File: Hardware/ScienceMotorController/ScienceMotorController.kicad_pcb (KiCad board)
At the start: 2 copper layers, 124.5 x 108.5 mm, 128 parts, among them SW1 Molex_SL_02, SW2 Molex_SL_02, SW3 Molex_SL_02, SW4 Molex_SL_02, SW5 Molex_SL_02, SW6 Molex_SL_02, U1 LT1910, U10 PMN280ENEAX, U11 TB67H400AFNG,EL, U12 TB67H400AFNG,EL, U13 LT1910, U14 PMN280ENEAX, U15 LTC6900, U16 TB67H400AFNG,EL, U17 TB67H400AFNG,EL, U2 OKI, U3 OKI, U4 OKI, U5 TB67H400AFNG,EL, U6 TB67H400AFNG,EL, U7 PMN280ENEAX, U8 LT1910, U9 TM4C129E_Launchpad

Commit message: deleted extra LEDs and Resistors. Generated and loaded new netlist.
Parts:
- removed D13, D21, D3, D6: LED, LED_SMD:LED_0603_1608Metric_Pad1.05x0.95mm_HandSolder
- removed R13, R23, R36: 3.3k, Resistor_SMD:R_0603_1608Metric_Pad1.05x0.95mm_HandSolder
- removed R4: 330, Resistor_SMD:R_0603_1608Metric_Pad1.05x0.95mm_HandSolder
- moved D16 128.3 mm to (125.2, 95.4), turned to 270 degrees
- moved D15 0.25 mm to (144.7, 96.0)
- moved R21 0.25 mm to (144.7, 92.5)
- renumbered Encode1 to AbsEncode1, Encode2 to AbsEncode2, Encode3 to AbsEncode3, Encode4 to AbsEncode4, Encode5 to AbsEncode5, SW1 to LimSwitch1, SW2 to LimSwitch2, SW3 to LimSwitch3, SW4 to LimSwitch4, SW5 to LimSwitch5, SW6 to LimSwitch6
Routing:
- net Net-(Conn2-Pad2): track 24.8 -> 23.5 mm

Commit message: more connections made, beginning to connect moco ICs
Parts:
- added REF**: 4_40_Hole, MRDT_Drill_Holes:4_40_Hole_Corner, F.Cu at (147.1, 84.3)
- added REF**: 4_40_Hole, MRDT_Drill_Holes:4_40_Hole_Corner, F.Cu at (38.8, 84.3)
- added REF**: 4_40_Hole, MRDT_Drill_Holes:4_40_Hole_Corner, F.Cu at (147.2, 176.6)
- added REF**: 4_40_Hole, MRDT_Drill_Holes:4_40_Hole_Corner, F.Cu at (38.8, 176.6)
- moved R8 293.3 mm to (21.3, 96.1)
- moved R7 236.5 mm to (21.1, 99.4)
- moved C9 216.9 mm to (83.4, 146.2), turned to 270 degrees
- moved R31 186.4 mm to (99.9, 146.2), turned to 270 degrees
- moved R22 181.5 mm to (128.8, 92.0), turned to 270 degrees
- moved R5 166.0 mm to (63.4, 152.7), turned to 180 degrees
- moved C11 165.1 mm to (98.2, 146.2), turned to 270 degrees
- moved R20 160.3 mm to (85.2, 146.2), turned to 270 degrees
- moved D4 149.5 mm to (66.9, 152.7), turned to 180 degrees
- moved R14 108.5 mm to (186.1, 150.0), turned to 90 degrees
- moved D7 106.7 mm to (184.3, 150.0), turned to 270 degrees
- moved R24 97.5 mm to (189.3, 159.4), turned to 180 degrees
- moved D14 97.3 mm to (189.4, 157.6), turned to 0 degrees
- moved R17 71.2 mm to (63.4, 154.3)
- moved D10 67.9 mm to (66.9, 154.3), turned to 180 degrees
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- renumbered LimSwitch2 to SW2, LimSwitch3 to SW3, LimSwitch5 to SW5, LimSwitch6 to SW6, LimSwitch1 to SW`1, LimSwitch4 to Sw45
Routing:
- net +5VA: track 25.1 -> 90.4 mm, vias 1 -> 2
- net +5V: track 204.5 -> 254.4 mm, vias 11 -> 15
- net +12V: track 154.0 -> 158.8 mm, vias 3 -> 5
- net Net-(R37-Pad2): track 4.01 -> 0.20 mm
- net Limit_Switch_1: track 115.8 -> 112.1 mm
- net Net-(R24-Pad2): track 3.61 -> 0.00 mm
- net Net-(R14-Pad2): track 3.56 -> 0.00 mm
- net +3V3: track 115.7 -> 119.1 mm
- net Oscillator: track 141.9 -> 139.2 mm, vias 10 -> 8
- net Net-(C9-Pad1): track 0.00 -> 2.56 mm
- net Net-(C11-Pad1): track 0.00 -> 2.56 mm
- net Limit_Switch_2: track 111.5 -> 109.0 mm
- net Net-(R20-Pad1): track 0.00 -> 2.41 mm
- net Net-(R31-Pad1): track 0.00 -> 2.35 mm
- net Net-(D16-Pad1): track 0.00 -> 2.03 mm
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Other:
- outline, holes or cut-outs redrawn
- board text added: "+12V"
- board text added: "+3V3"
- board text added: "+5V"
- board text added: "+5VA"
- board text added: "Power Indicators"
- board text removed: "+3V3 Indicator"
- board text removed: "+5V Indicator"
- board text removed: "+5VA Indicator"

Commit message: resistors on moco chips added.
Had changed netlist to try a different placement for the motor LEDs, but reverted to original position
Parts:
- removed REF** (x4): 4_40_Hole, MRDT_Drill_Holes:4_40_Hole_Corner
- moved D1 230.0 mm to (54.5, 97.8), turned to 180 degrees
- moved R45 221.8 mm to (72.2, 104.9)
- moved R1 221.0 mm to (54.5, 99.6)
- moved R46 212.5 mm to (72.2, 103.1)
- moved R41 211.3 mm to (72.2, 99.6)
- moved R9 210.2 mm to (54.5, 101.3)
- moved R40 199.9 mm to (90.5, 99.6)
- moved R47 196.5 mm to (72.2, 101.3)
- moved R44 194.3 mm to (90.5, 101.3)
- moved R11 189.2 mm to (109.0, 103.1)
- moved R30 187.4 mm to (127.4, 101.3)
- moved R2 181.3 mm to (109.0, 99.6)
- moved D26 177.9 mm to (72.2, 97.8), turned to 180 degrees
- moved R10 174.6 mm to (109.0, 104.9)
- moved R28 170.5 mm to (127.4, 104.9)
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- renumbered SW`1 to LimSwitch1, SW2 to LimSwitch2, SW3 to LimSwitch3, Sw45 to LimSwitch4, SW5 to LimSwitch5, SW6 to LimSwitch6
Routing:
- net +5V: track 254.4 -> 164.5 mm
- net Oscillator: track 139.2 -> 52.2 mm, vias 8 -> 7
- net GND: track 169.7 -> 182.5 mm
- net Net-(Conn4-Pad1): track 8.59 -> 20.1 mm
- net Net-(R7-Pad1): track 0.00 -> 3.23 mm
- net Net-(R10-Pad1): track 0.00 -> 3.21 mm
- net Net-(R28-Pad1): track 0.00 -> 3.09 mm
- net Net-(R25-Pad1): track 0.00 -> 3.03 mm
- net Net-(R26-Pad1): track 0.00 -> 3.01 mm
- net Net-(R45-Pad1): track 0.00 -> 2.98 mm
- net Net-(R42-Pad1): track 0.00 -> 2.96 mm
- net Net-(Conn6-Pad2): track 20.4 -> 23.1 mm
- net Net-(Conn1-Pad2): track 21.4 -> 24.2 mm
- net Net-(R47-Pad1): track 0.00 -> 2.66 mm
- net Net-(R30-Pad1): track 0.00 -> 2.63 mm
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
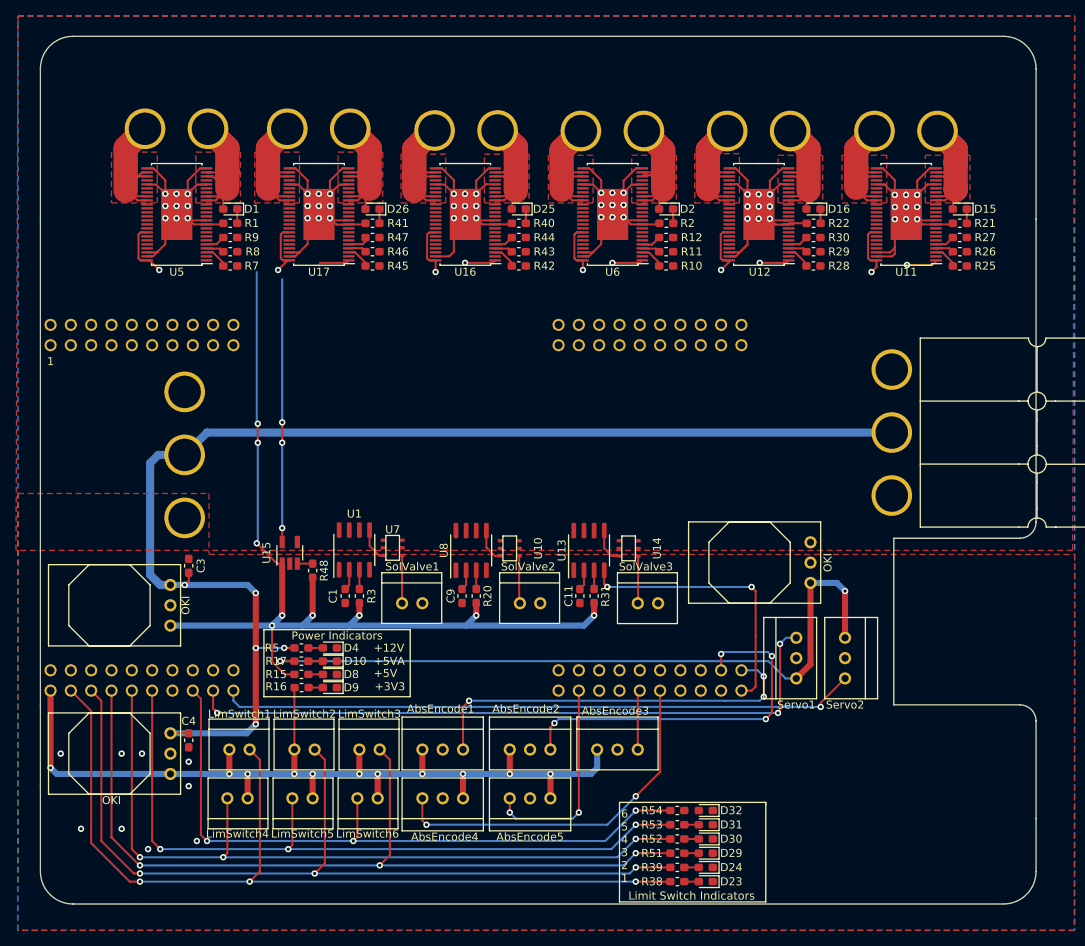
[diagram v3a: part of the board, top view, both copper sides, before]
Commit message: finished moco alignment
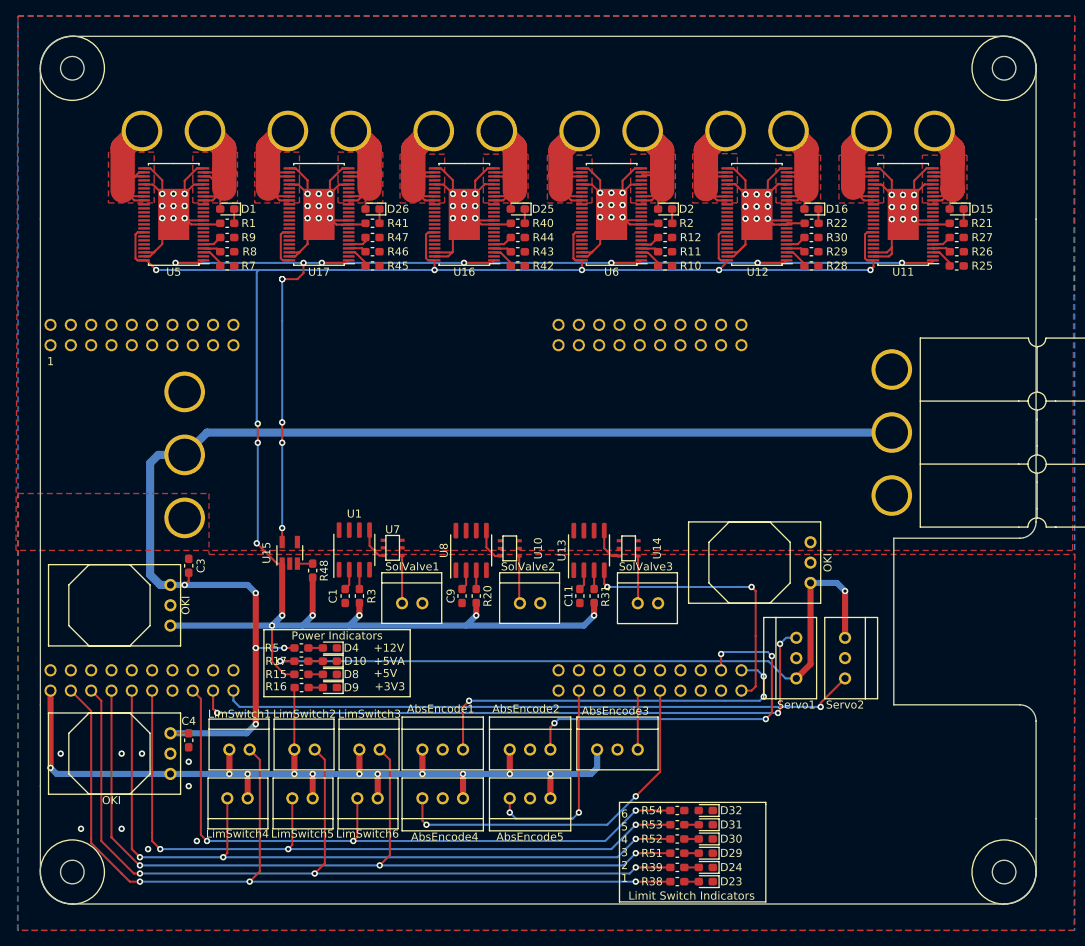
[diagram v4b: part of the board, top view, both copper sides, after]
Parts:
- added REF**: 4_40_Hole, MRDT_Drill_Holes:4_40_Hole_Corner, F.Cu at (147.2, 176.7)
- added REF**: 4_40_Hole, MRDT_Drill_Holes:4_40_Hole_Corner, F.Cu at (38.7, 176.7)
- added REF**: 4_40_Hole, MRDT_Drill_Holes:4_40_Hole_Corner, F.Cu at (38.7, 84.2)
- added REF**: 4_40_Hole, MRDT_Drill_Holes:4_40_Hole_Corner, F.Cu at (147.2, 84.2)
- moved Conn1 0.47 mm to (43.4, 88.0)
- moved Conn2 0.38 mm to (134.6, 88.0)
- moved D1 0.38 mm to (54.1, 97.8)
- moved D15 0.38 mm to (145.3, 97.8)
- moved R1 0.38 mm to (54.1, 99.6)
- moved R21 0.38 mm to (145.3, 99.6)
- moved R25 0.38 mm to (145.3, 104.9)
- moved R26 0.38 mm to (145.3, 103.1)
- moved R27 0.38 mm to (145.3, 101.3)
- moved R7 0.38 mm to (54.1, 104.9)
- moved R8 0.38 mm to (54.1, 103.1)
- moved R9 0.38 mm to (54.1, 101.3)
- moved U11 0.38 mm to (138.6, 98.5)
- moved U5 0.38 mm to (47.4, 98.5)
- moved Conn6 0.29 mm to (61.7, 88.0)
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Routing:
- net Oscillator: track 52.2 -> 151.0 mm, vias 7 -> 12
- net +5V: track 164.5 -> 252.0 mm, vias 15 -> 14
- net GND: track 182.5 -> 185.7 mm

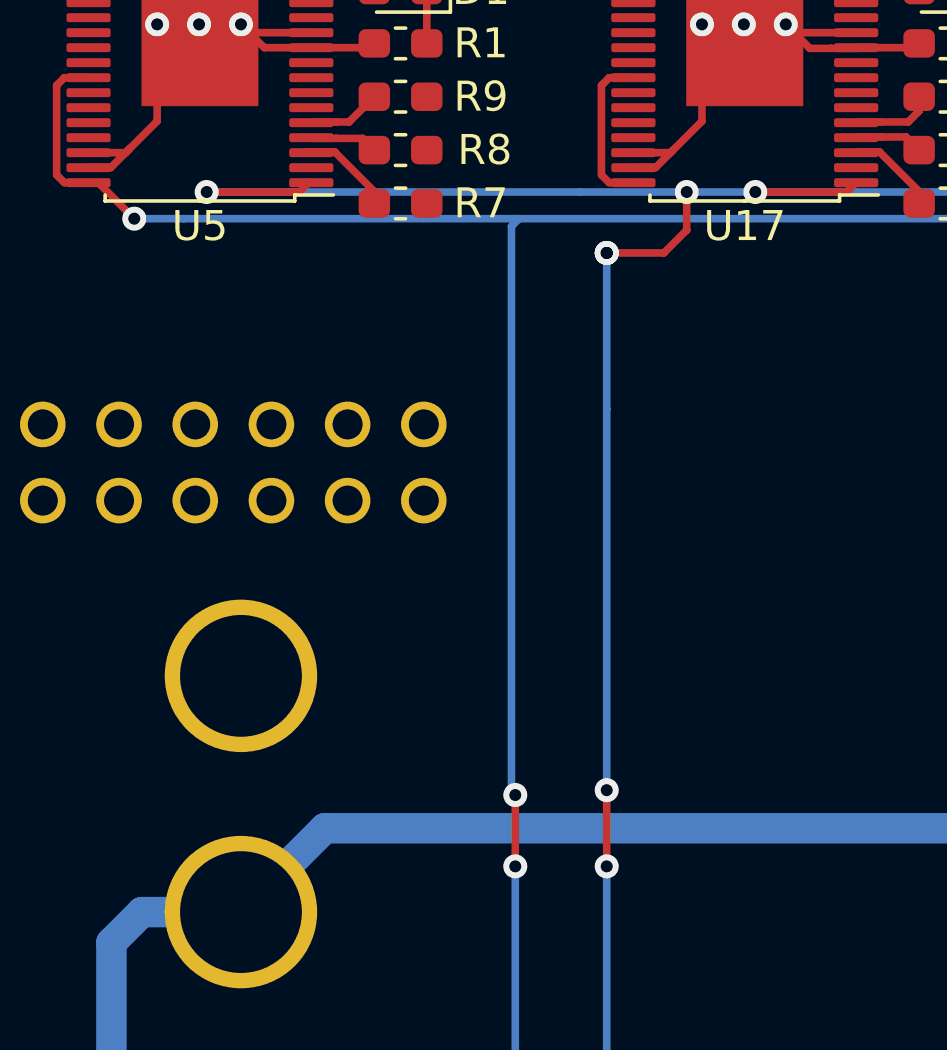
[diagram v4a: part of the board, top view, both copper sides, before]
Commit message: connected 5V and osc. buses to moco ICs. Updated netlist to have pins closer to tiva pins
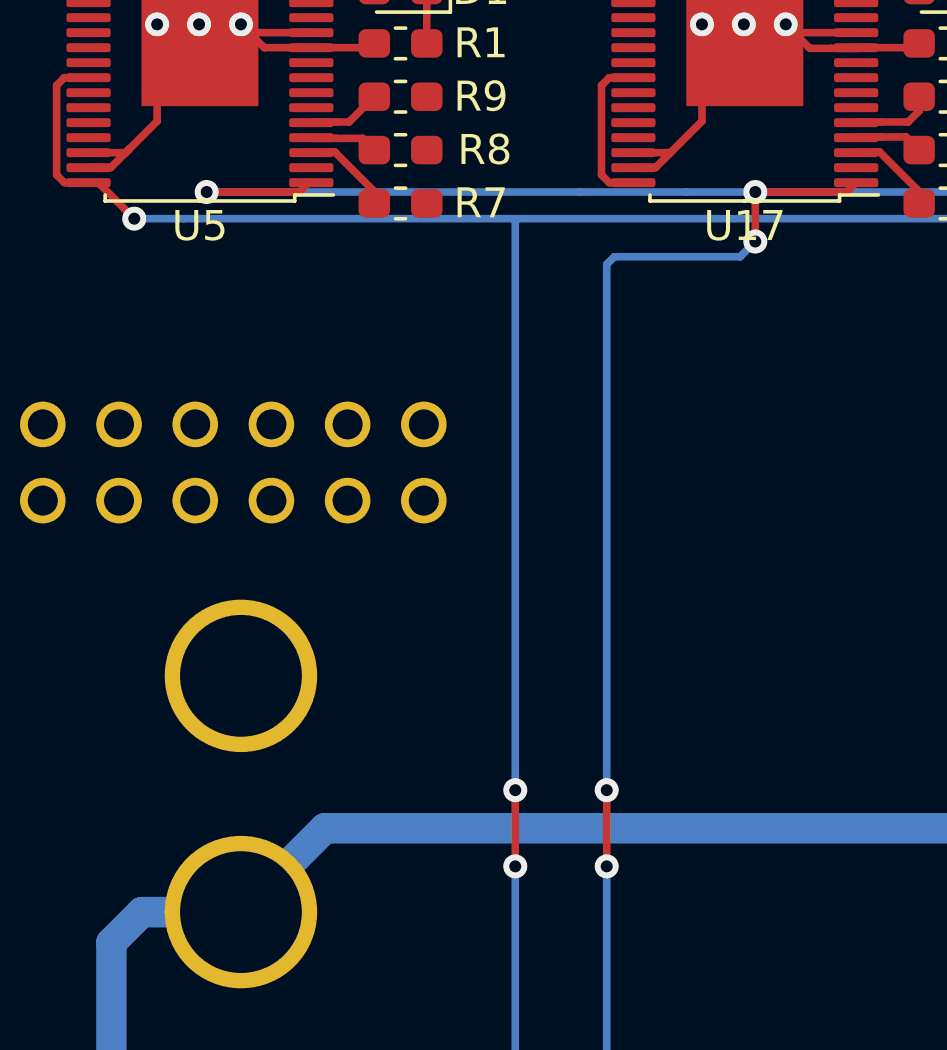
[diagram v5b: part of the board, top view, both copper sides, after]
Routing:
- net Oscillator: track 151.0 -> 153.2 mm, vias 12 -> 10

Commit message: continued connecting caps and resistors. Moved around some Tiva pins for the moco ICs
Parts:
- removed REF** (x4): 4_40_Hole, MRDT_Drill_Holes:4_40_Hole_Corner
- moved C7 227.4 mm to (47.9, 172.1)
- moved C2 196.6 mm to (95.4, 138.3), turned to 270 degrees
- moved C12 189.9 mm to (66.2, 138.3), turned to 270 degrees
- moved C10 189.3 mm to (80.8, 138.4), turned to 270 degrees
- moved C13 188.1 mm to (49.5, 152.0), turned to 270 degrees
- moved R6 185.8 mm to (63.4, 151.0), turned to 180 degrees
- moved D5 176.2 mm to (66.9, 151.0), turned to 180 degrees
- moved C5 117.0 mm to (131.1, 140.8), turned to 270 degrees
- moved C8 116.4 mm to (130.4, 144.3)
- moved R14 106.7 mm to (79.4, 151.1), turned to 180 degrees
- moved D7 105.0 mm to (79.4, 152.9), turned to 0 degrees
- moved R24 95.6 mm to (94.1, 151.1)
- moved D14 95.4 mm to (94.1, 152.9)
- moved C6 64.9 mm to (237.3, 106.8)
- moved R32 64.9 mm to (203.5, 136.4)
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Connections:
- U9 pad PB4: Net-(U9-PadPB4) -> Solenoid_Valve_1
- U9 pad PB5: Net-(U9-PadPB5) -> Solenoid_Valve_2
- U9 pad PF1: InA2_2 -> InA2_1
- U9 pad PF2: InA1_2 -> InA1_1
- U9 pad PF3: InA2_3 -> InA1_6
- U9 pad PG0: InA1_3 -> InA2_6
- U9 pad PG1: InA1_1 -> InA1_2
- U9 pad PH0: InA2_5 -> InA2_4
- U9 pad PH1: InA1_5 -> InA1_4
- U9 pad PK0: Net-(U9-PadPK0) -> Solenoid_Valve_3
- U9 pad PK4: InA2_1 -> InA2_2
- U9 pad PK6: InA1_6 -> InA2_5
- U9 pad PK7: InA2_6 -> InA1_5
- U9 pad PL0: InA2_4 -> InA2_3
- U9 pad PL1: InA1_4 -> InA1_3
- U9 pad PL4: PWMA_2 -> PWMA_1
- U9 pad PL5: PWMA_3 -> PWMA_6
- U9 pad PM0: PWMA_5 -> PWMA_2
- U9 pad PM1: PWMA_6 -> PWMA_3
- U9 pad PM2: PWMA_1 -> PWMA_5
- U9 pad PN4: Solenoid_Valve_3 -> Net-(U9-PadPN4)
- U9 pad PN5: Solenoid_Valve_2 -> Net-(U9-PadPN5)
- U9 pad PP4: Solenoid_Valve_1 -> Net-(U9-PadPP4)
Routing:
- net InA2_1: track 0.00 -> 41.4 mm, vias 0 -> 1
- net Solenoid_Valve_1: track 0.00 -> 40.5 mm, vias 0 -> 2
- net +5V: track 251.8 -> 289.2 mm, vias 14 -> 13
- net PWMA_1: track 0.00 -> 35.1 mm, vias 0 -> 2
- net InA1_1: track 0.35 -> 34.1 mm, vias 0 -> 1
- net Solenoid_Valve_2: track 0.00 -> 28.5 mm, vias 0 -> 2
- net Solenoid_Valve_3: track 34.9 -> 16.0 mm
- net +12VA: track 0.00 -> 16.5 mm, vias 0 -> 7
- net GND: track 185.7 -> 199.5 mm, vias 63 -> 79
- net Net-(R24-Pad2): track 0.00 -> 4.06 mm
- net Net-(R14-Pad2): track 0.00 -> 4.06 mm
- net Net-(R37-Pad2): track 0.20 -> 4.01 mm
- net +3V3: track 119.1 -> 122.8 mm
- net Encoder_PWM_1: track 49.1 -> 46.4 mm, vias 3 -> 1
- net +5VA: track 90.4 -> 93.1 mm
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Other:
- board text added: "+"
- board text added: "+12VA"
- board text added: "-"
- board text added: "Connector Pinouts"
- board text added: "Encoder & Servo"
- board text added: "Limit Switch"
- board text added: "S"

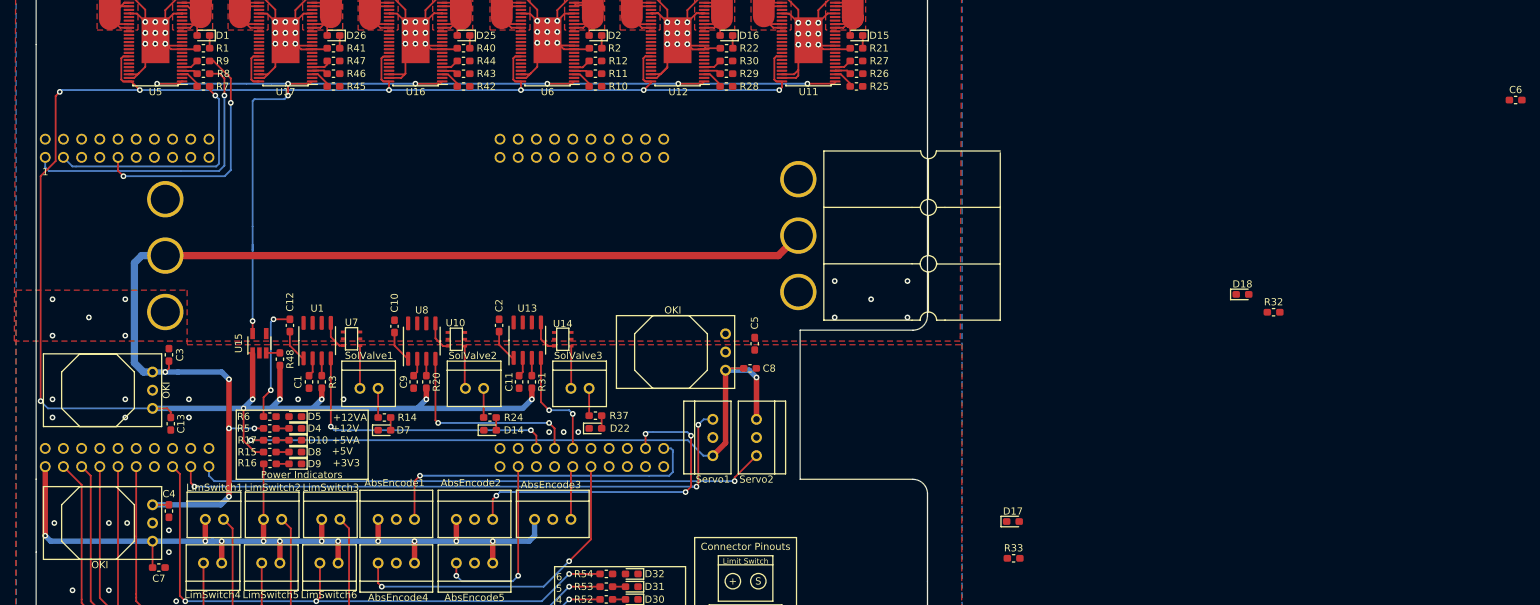
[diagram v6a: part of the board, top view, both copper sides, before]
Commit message: began reworking moco IC control traces. Will need to rearrange the netlist to reduce complexity of traces
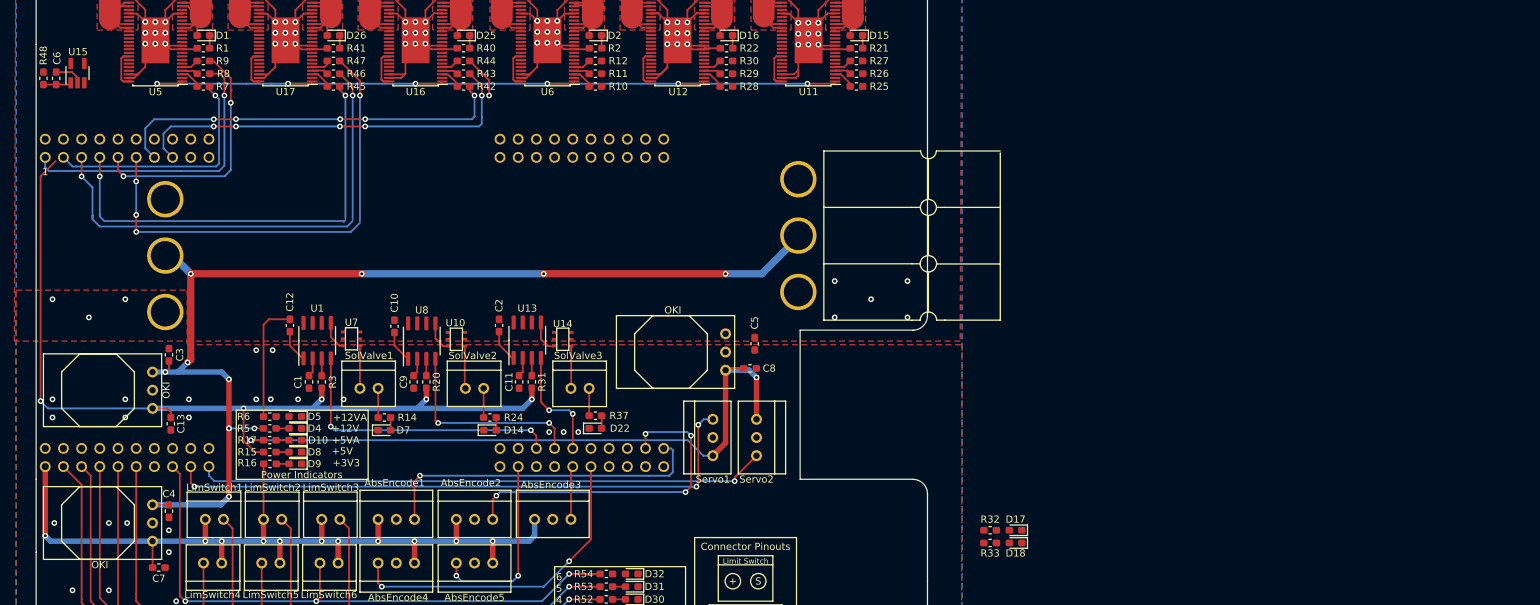
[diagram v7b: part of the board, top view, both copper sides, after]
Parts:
- moved C6 203.8 mm to (33.5, 103.8), turned to 90 degrees
- moved R48 51.3 mm to (31.8, 103.8)
- moved R32 49.9 mm to (163.9, 166.9), turned to 180 degrees
- moved D18 47.0 mm to (167.5, 168.7), turned to 180 degrees
- moved U15 45.5 mm to (36.5, 103.0)
- moved R33 3.91 mm to (163.9, 168.7), turned to 180 degrees
- moved D17 1.28 mm to (167.5, 166.9), turned to 180 degrees
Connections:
- U9 pad PF3: InA1_6 -> InA2_6
- U9 pad PG0: InA2_6 -> InA1_6
- U9 pad PL0: InA2_3 -> InA1_3
- U9 pad PL1: InA1_3 -> InA2_3
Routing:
- net +5V: track 289.2 -> 160.4 mm, vias 13 -> 5
- net InA2_6: track 0.00 -> 67.6 mm, vias 0 -> 2
- net PWMA_6: track 0.00 -> 65.7 mm, vias 0 -> 4
- net InA1_6: track 0.00 -> 61.8 mm, vias 0 -> 2
- net InA2_3: track 0.00 -> 56.5 mm, vias 0 -> 5
- net InA1_3: track 0.00 -> 55.7 mm, vias 0 -> 5
- net Oscillator: track 153.9 -> 113.6 mm, vias 8 -> 6
- net PWMA_3: track 0.00 -> 5.94 mm, vias 0 -> 1
- net +12V: track 158.8 -> 153.5 mm, vias 5 -> 10
- net GND: track 199.5 -> 203.6 mm, vias 79 -> 81
- net Net-(R48-Pad1): track 1.91 -> 0.00 mm
- net +12VA: track 16.5 -> 16.7 mm, vias 7 -> 5
